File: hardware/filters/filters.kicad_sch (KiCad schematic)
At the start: 47 parts

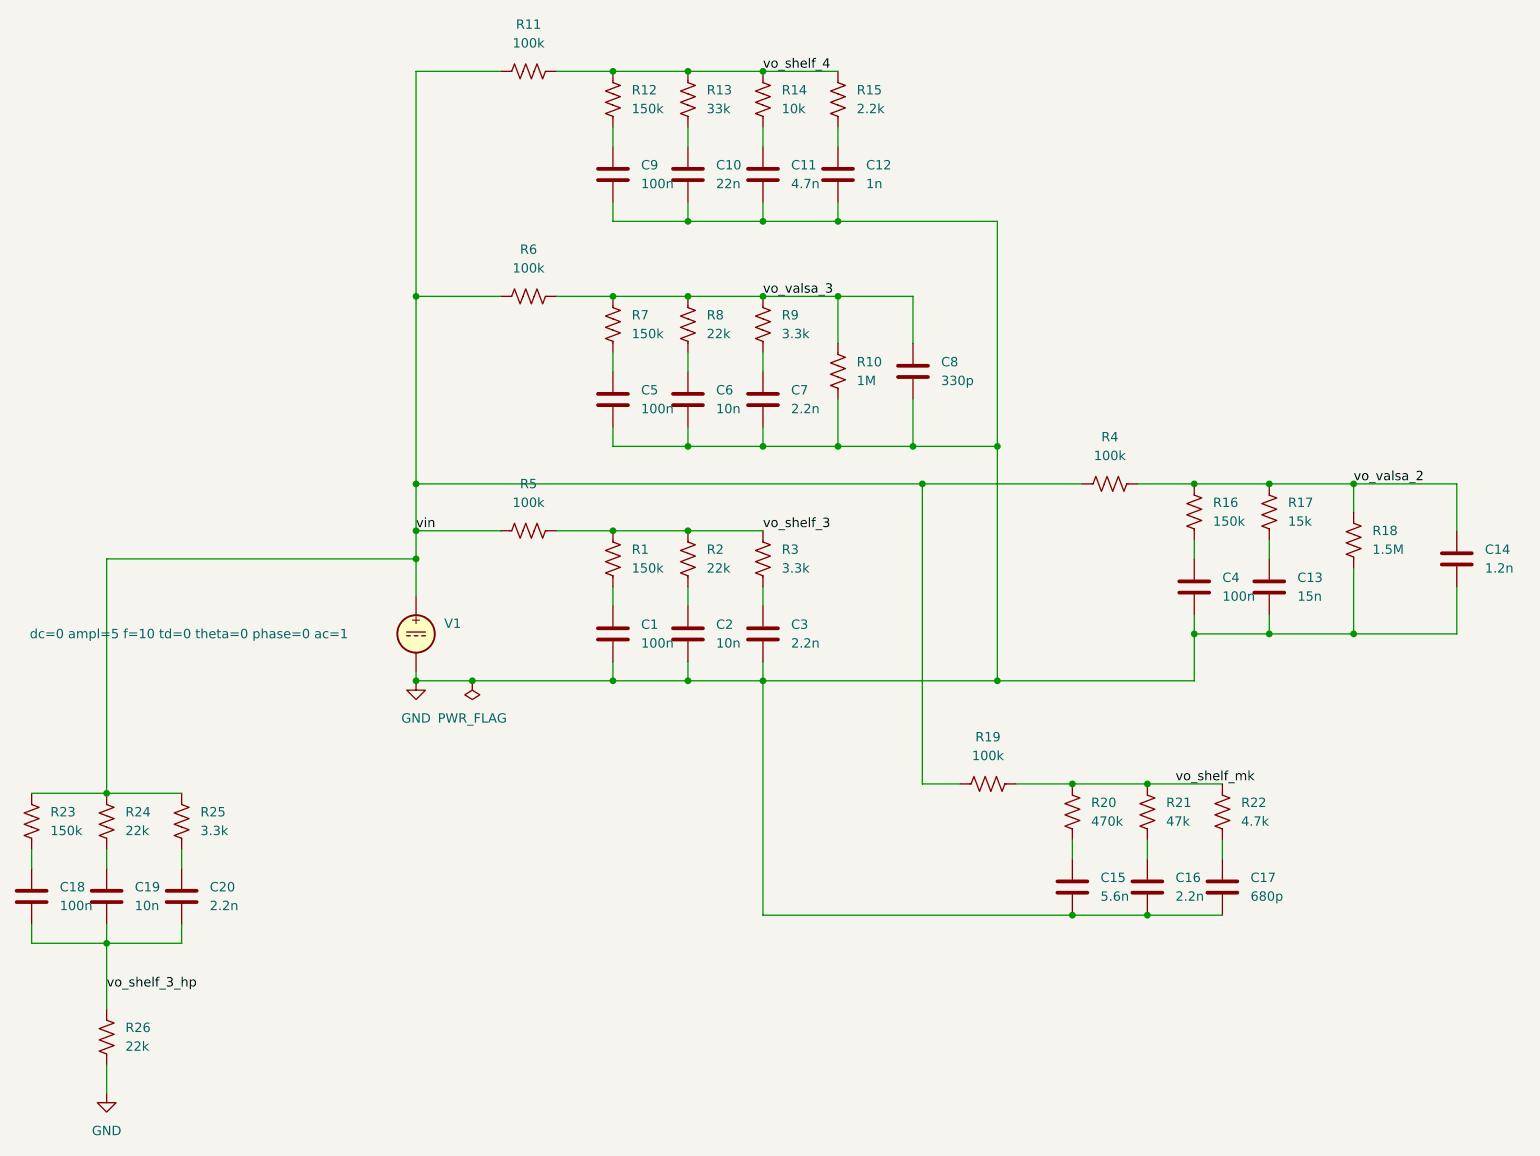
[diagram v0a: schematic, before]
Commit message: finished design checks on grain output and update schematic/layout to v1.1
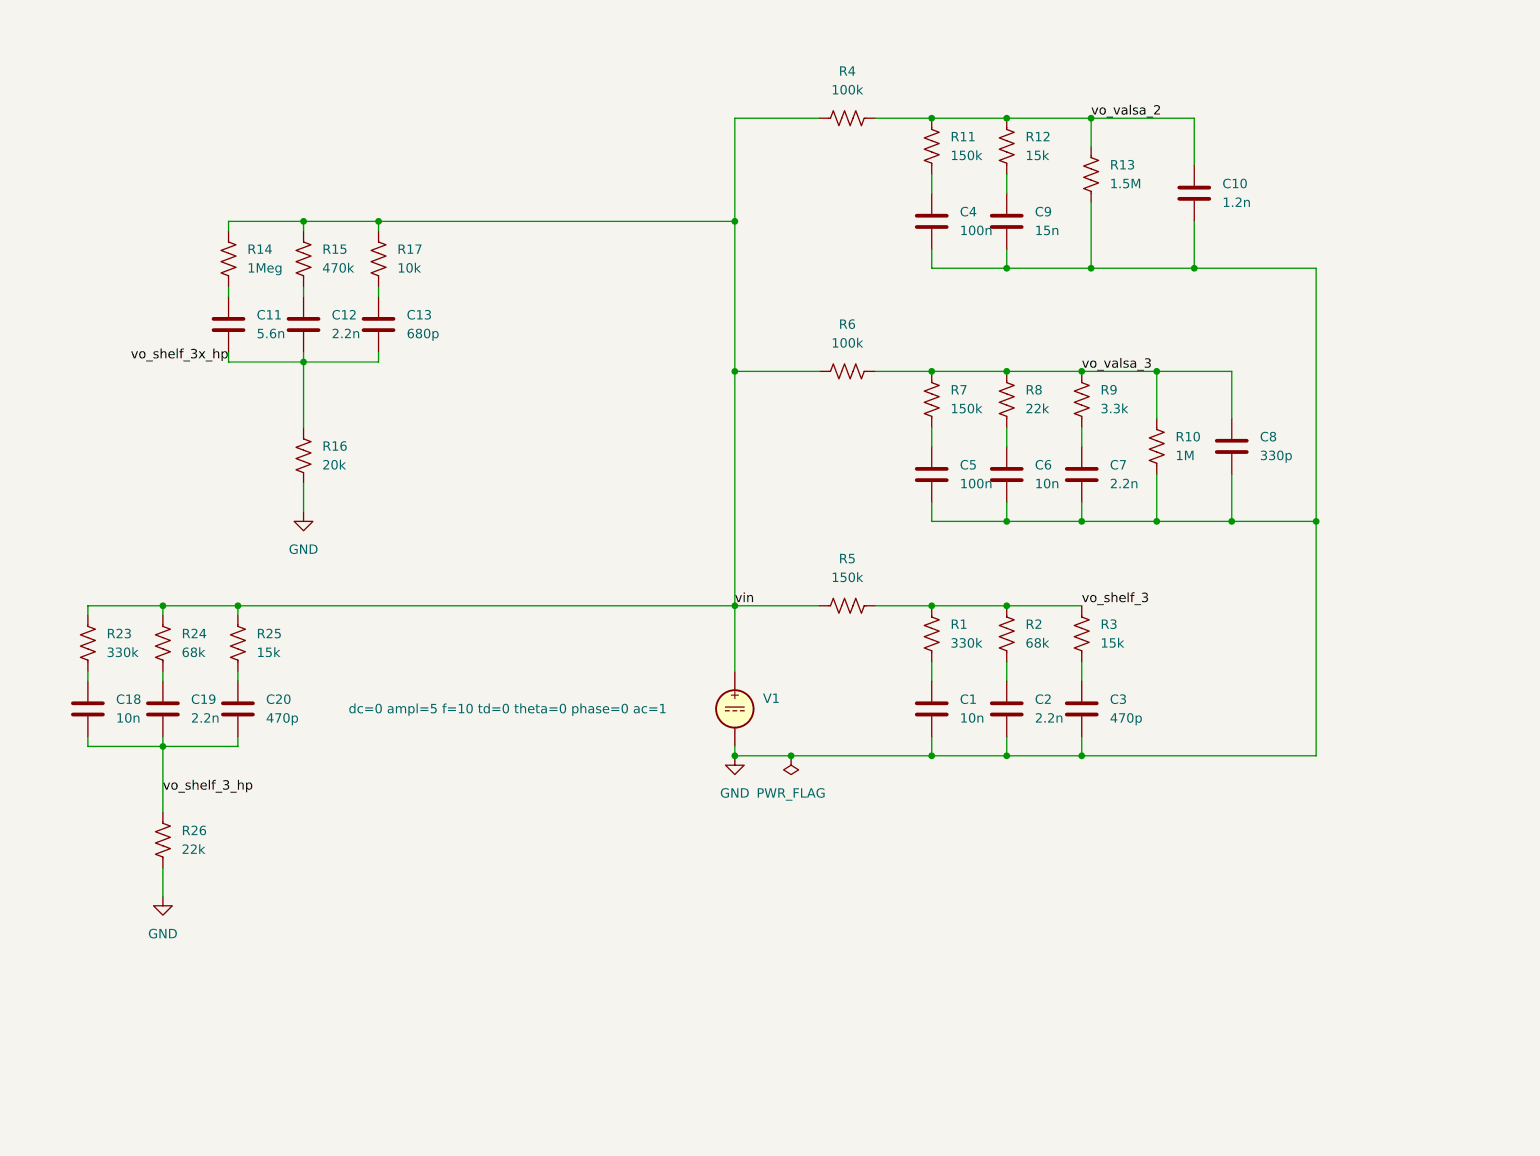
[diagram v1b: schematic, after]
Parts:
- removed C14: 1.2n, symbol Device:C
- removed C15: 5.6n, symbol Device:C
- removed C16: 2.2n, symbol Device:C
- removed C17: 680p, symbol Device:C
- removed R18: 1.5M, symbol Device:R_US
- removed R19: 100k, symbol Device:R_US
- removed R20: 470k, symbol Device:R_US
- removed R21: 47k, symbol Device:R_US
- removed R22: 4.7k, symbol Device:R_US
- C1, C18: value 100n -> 10n
- C10: value 22n -> 1.2n
- C11: value 4.7n -> 5.6n
- C12: value 1n -> 2.2n
- C13: value 15n -> 680p
- C19, C2: value 10n -> 2.2n
- C20, C3: value 2.2n -> 470p
- C9: value 100n -> 15n
- R1, R23: value 150k -> 330k
- R11, R5: value 100k -> 150k
- R12: value 150k -> 15k
- R13: value 33k -> 1.5M
- R14: value 10k -> 1Meg
- R15: value 2.2k -> 470k
- R16: value 150k -> 20k
- R17: value 15k -> 10k
- R2, R24: value 22k -> 68k
- R25, R3: value 3.3k -> 15k
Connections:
- net GND: now also R13.2, R16.2; no longer C11.2, C12.2, C13.2
- net vin: now also R14.1, R15.1, R17.1; no longer R11.1
- net vo_valsa_2: now also C10.1, R11.1, R12.1, R13.1; no longer R16.1, R17.1
- net at C4.1: now also R11.2; no longer R16.2
- removed net vo_shelf_4: R11.2, R12.1, R13.1, R14.1, R15.1
- new net vo_shelf_3x_hp: C11.2, C12.2, C13.2, R16.1
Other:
- moved on the sheet: C1, C18, C19, C2, C20, C3, C5, C6, C7, C8, R1, R10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
